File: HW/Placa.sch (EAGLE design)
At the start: 13 parts, among them IC1 7805TV

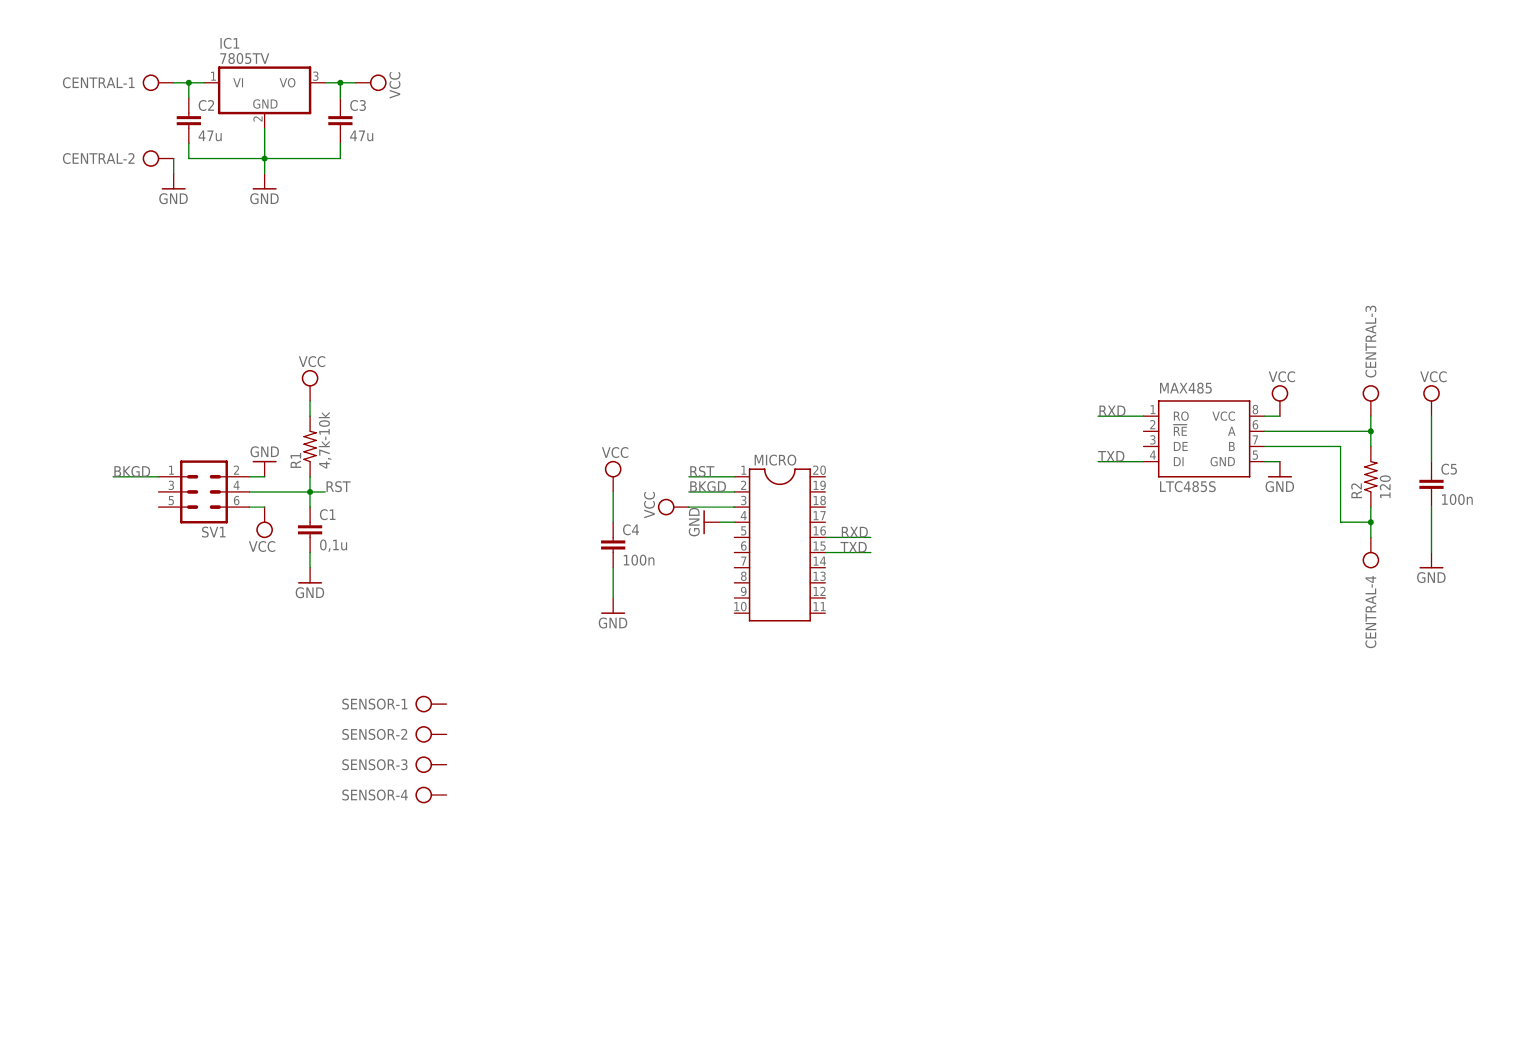
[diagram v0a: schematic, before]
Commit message: Proyecto Eagle
Subo el esquematico con los cambios realizados el 17/05/2018
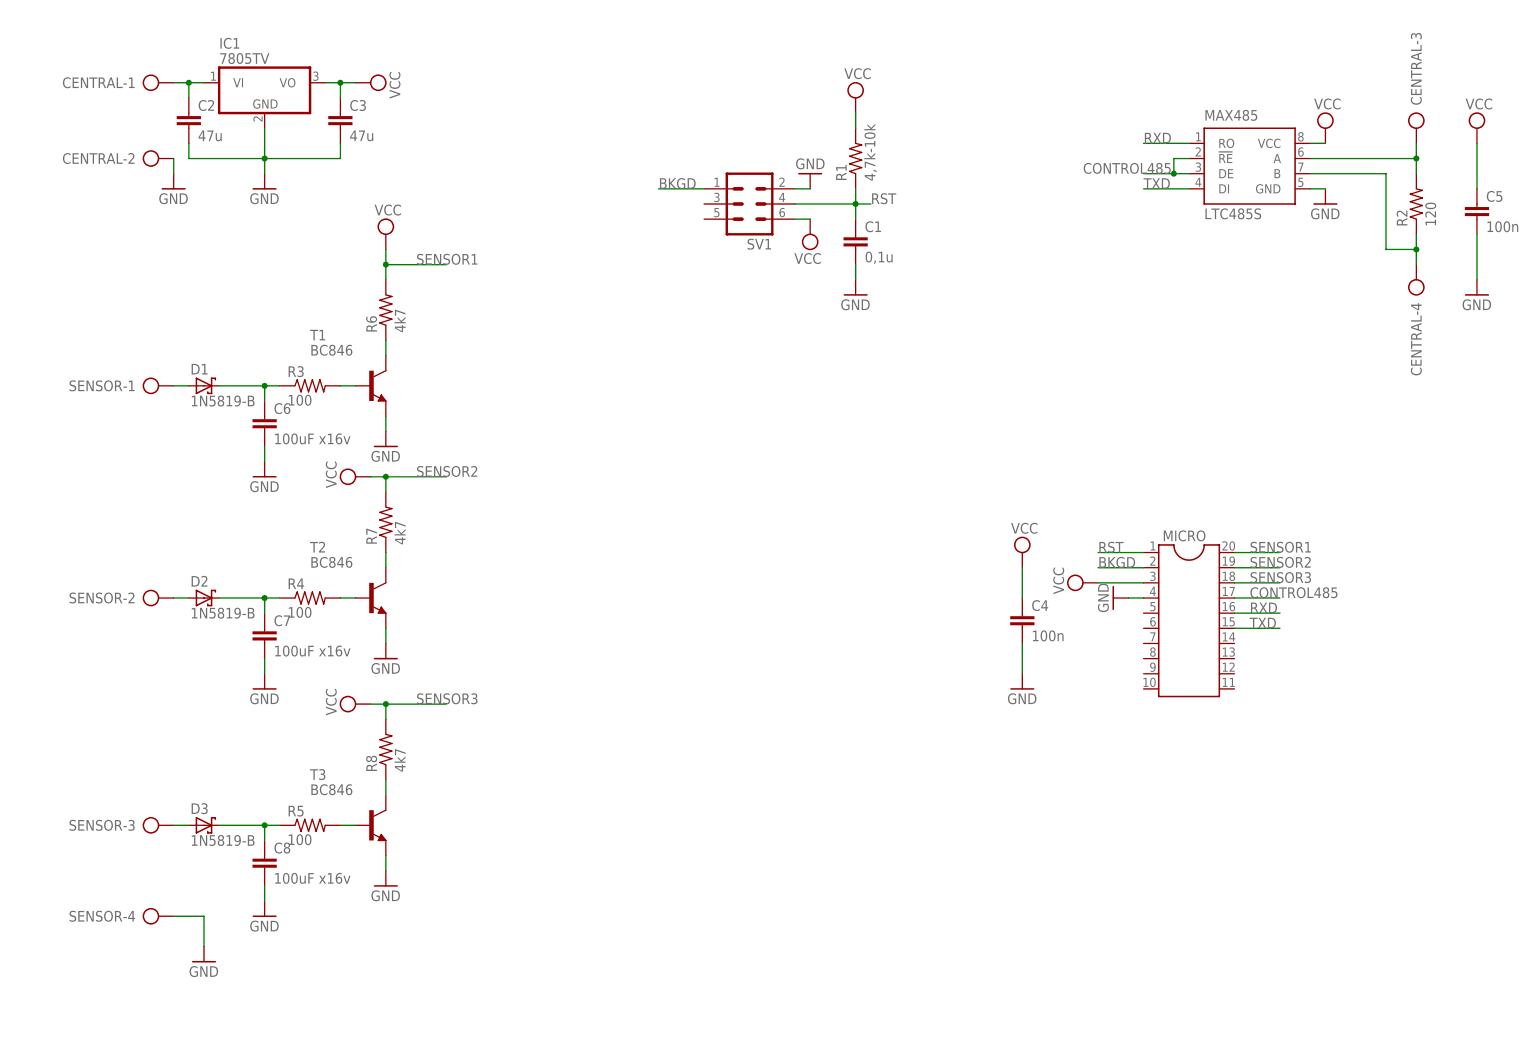
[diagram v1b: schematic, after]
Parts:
- added C6, C7, C8: 100uF x16v, resistor:C-EU025-025X050
- added D1, D2, D3: 1N5819-B, diode:1N5819-B
- added R3, R4, R5: 100, resistor:R-US_R0805
- added R6, R7, R8: 4k7, resistor:R-US_R0805
- added T1, T2, T3: BC846, transistor:BC846
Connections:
- new net CONTROL485: MAX485.!RE, MAX485.DE, MICRO.17
- new net N$10: R5.2, T3.B
- new net N$11: R8.1, T3.C
- new net N$12: R4.2, T2.B
- new net N$13: R7.1, T2.C
- new net N$14: R3.2, T1.B
- new net N$15: R6.1, T1.C
- new net N$4: D1.A, SENSOR-1.KL
- new net N$5: D2.A, SENSOR-2.KL
- new net N$6: D3.A, SENSOR-3.KL
- new net N$7: C6.1, D1.C, R3.1
- new net N$8: C7.1, D2.C, R4.1
- new net N$9: C8.1, D3.C, R5.1
- new net SENSOR1: MICRO.20, R6.2
- new net SENSOR2: MICRO.19, R7.2
- new net SENSOR3: MICRO.18, R8.2
- net GND: now also C6.2, C7.2, C8.2, SENSOR-4.KL, T1.E, T2.E, T3.E
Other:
- moved on the sheet: C1, C4, C5, CENTRAL-3, CENTRAL-4, MAX485, MICRO, R1, R2, SENSOR-1, SENSOR-2, SENSOR-3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

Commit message: Correcciones SCH
Algunas correcciones, falta revisión final.
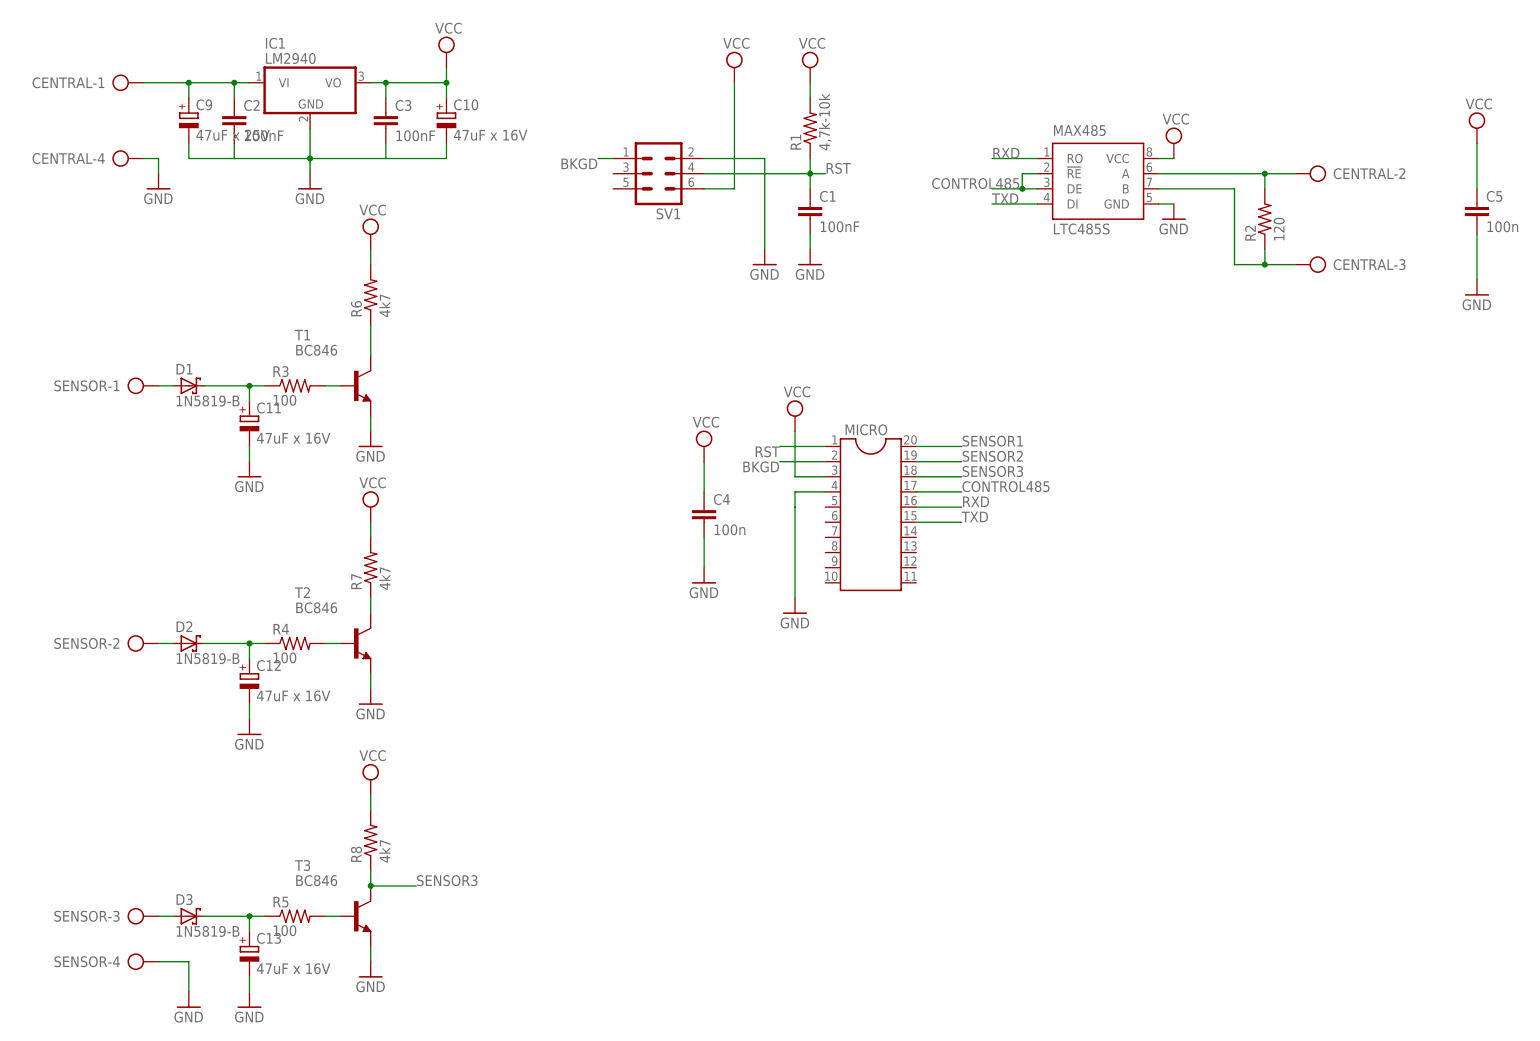
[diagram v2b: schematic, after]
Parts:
- removed C6, C7, C8: 100uF x16v, resistor:C-EU025-025X050
- added C10, C11, C12, C13: 47uF x 16V, rcl:CPOL-EUE2,5-6E
- added C9: 47uF x 25V, rcl:CPOL-EUE2,5-6E
- C1: value 0,1u -> 100nF
- C2, C3: value 47u -> 100nF
- IC1: value 7805TV -> LM2940
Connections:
- removed net N$11: R8.1, T3.C
- net GND: now also C10.-, C11.-, C12.-, C13.-, C9.-, CENTRAL-4.KL; no longer C6.2, C7.2, C8.2, CENTRAL-2.KL
- net N$1: now also C9.+
- net N$2: now also CENTRAL-2.KL; no longer CENTRAL-3.KL
- net N$3: now also CENTRAL-3.KL; no longer CENTRAL-4.KL
- net N$7: now also C11.+; no longer C6.1
- net N$8: now also C12.+; no longer C7.1
- net N$9: now also C13.+; no longer C8.1
- net SENSOR1: no longer R6.2
- net SENSOR2: no longer R7.2
- net SENSOR3: now also R8.1, T3.C; no longer R8.2
- net VCC: now also C10.+, R6.2, R7.2, R8.2
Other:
- moved on the sheet: C1, C2, C3, C4, CENTRAL-1, CENTRAL-2, CENTRAL-3, CENTRAL-4, D1, D2, D3, IC1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

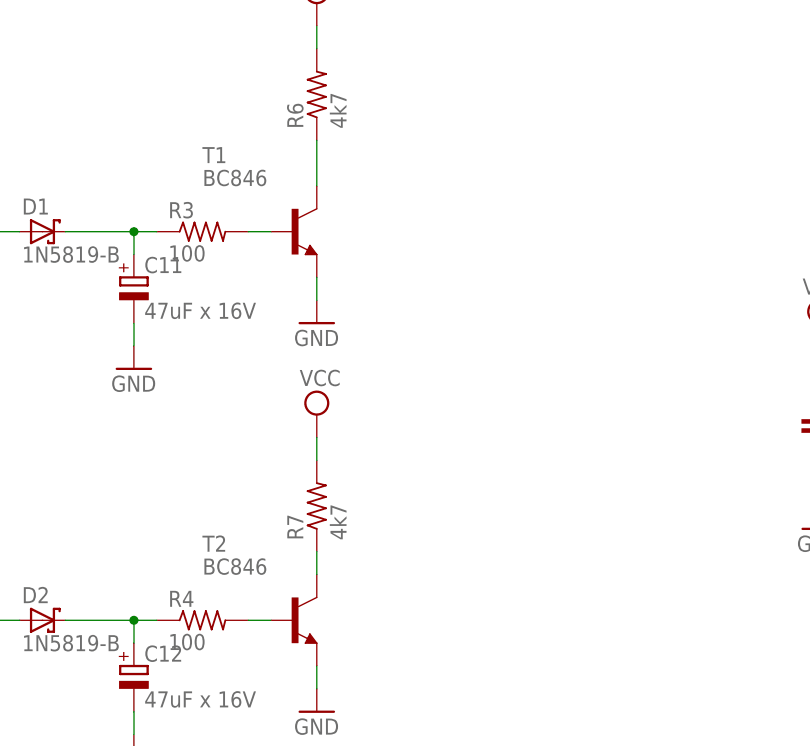
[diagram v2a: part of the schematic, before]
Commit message: Proyecto Eagle
Esquematico terminado
Board falta corregir errores
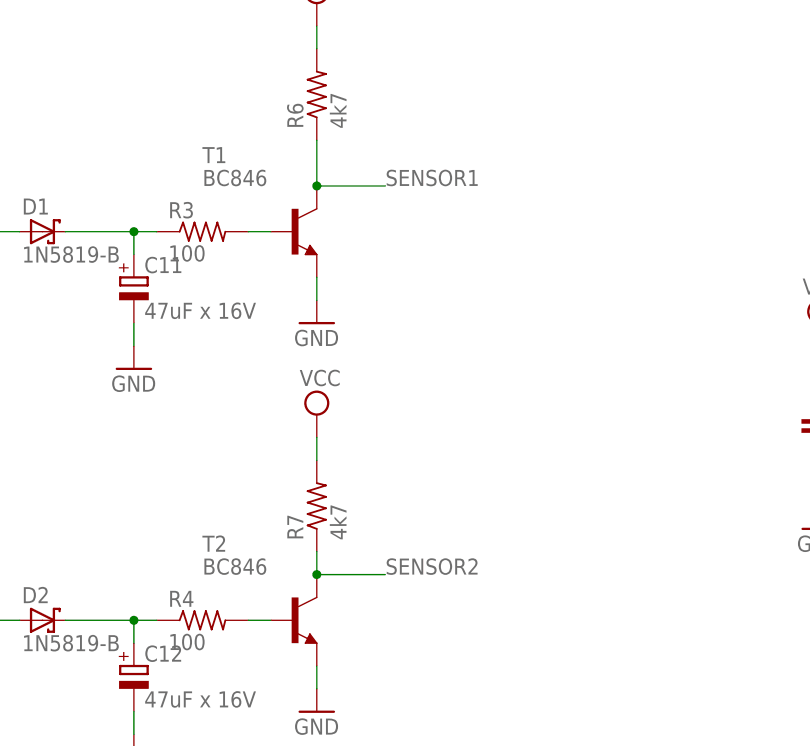
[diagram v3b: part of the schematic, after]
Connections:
- removed net N$13: R7.1, T2.C
- removed net N$15: R6.1, T1.C
- net SENSOR1: now also R6.1, T1.C
- net SENSOR2: now also R7.1, T2.C
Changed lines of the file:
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@@
 <?xml version="1.0" encoding="utf-8"?>
 <!DOCTYPE eagle SYSTEM "eagle.dtd">
-<eagle version="7.7.0">
+<eagle version="7.6.0">
 <drawing>
 <settings>
@@
 </segment>
 </net>
-<net name="N$13" class="0">
+<net name="N$14" class="0">
+<segment>
+<pinref part="R3" gate="G$1" pin="2"/>
+<pinref part="T1" gate="G$1" pin="B"/>
+<wire x1="5.08" y1="119.38" x2="7.62" y2="119.38" width="0.1524" layer="91"/>
+</segment>
+</net>
+<net name="SENSOR1" class="0">
+<segment>
+<pinref part="MICRO" gate="G$1" pin="20"/>
+<wire x1="104.14" y1="109.22" x2="111.76" y2="109.22" width="0.1524" layer="91"/>
+<label x="111.76" y="109.22" size="1.778" layer="95"/>
+</segment>
+<segment>
+<pinref part="T1" gate="G$1" pin="C"/>
+<pinref part="R6" gate="G$1" pin="1"/>
+<wire x1="12.7" y1="124.46" x2="12.7" y2="129.54" width="0.1524" layer="91"/>
+<label x="20.32" y="124.46" size="1.778" layer="95"/>
+<junction x="12.7" y="124.46"/>
+<wire x1="12.7" y1="124.46" x2="20.32" y2="124.46" width="0.1524" layer="91"/>
+</segment>
+</net>
+<net name="SENSOR2" class="0">
+<segment>
+<pinref part="MICRO" gate="G$1" pin="19"/>
+<wire x1="104.14" y1="106.68" x2="111.76" y2="106.68" width="0.1524" layer="91"/>
+<label x="111.76" y="106.68" size="1.778" layer="95"/>
+</segment>
 <segment>
 <pinref part="T2" gate="G$1" pin="C"/>
 <pinref part="R7" gate="G$1" pin="1"/>
 <wire x1="12.7" y1="81.28" x2="12.7" y2="83.82" width="0.1524" layer="91"/>
-</segment>
-</net>
-<net name="N$14" class="0">
-<segment>
-<pinref part="R3" gate="G$1" pin="2"/>
-<pinref part="T1" gate="G$1" pin="B"/>
-<wire x1="5.08" y1="119.38" x2="7.62" y2="119.38" width="0.1524" layer="91"/>
-</segment>
-</net>
-<net name="N$15" class="0">
-<segment>
-<pinref part="T1" gate="G$1" pin="C"/>
-<pinref part="R6" gate="G$1" pin="1"/>
-<wire x1="12.7" y1="124.46" x2="12.7" y2="129.54" width="0.1524" layer="91"/>
-</segment>
-</net>
-<net name="SENSOR1" class="0">
-<segment>
-<pinref part="MICRO" gate="G$1" pin="20"/>
-<wire x1="104.14" y1="109.22" x2="111.76" y2="109.22" width="0.1524" layer="91"/>
-<label x="111.76" y="109.22" size="1.778" layer="95"/>
-</segment>
-</net>
-<net name="SENSOR2" class="0">
-<segment>
-<pinref part="MICRO" gate="G$1" pin="19"/>
-<wire x1="104.14" y1="106.68" x2="111.76" y2="106.68" width="0.1524" layer="91"/>
-<label x="111.76" y="106.68" size="1.778" layer="95"/>
-</segment>
-</net>
+<label x="20.32" y="81.28" size="1.778" layer="95"/>
+<junction x="12.7" y="81.28"/>
+<wire x1="12.7" y1="81.28" x2="20.32" y2="81.28" width="0.1524" layer="91"/>
+</segment>
+</net>
